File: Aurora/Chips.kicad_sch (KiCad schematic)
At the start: 69 parts, among them J1 UJ20-C-H-C-3-SMT-TR, J2 DM3AT-SF-PEJM5, J3 Conn_Coaxial_Small, SW1 PCM12SMTR, U1 STM32H757BITx, U2 USBLC6-2SC6, U3 TPS2121RUXR, U4 AP63203QWU-7, U5 ICM-45686, U6 ICM-42688-P, U7 BNO085, U8 XBP9X-DMUS-021, U9 MCP23017T-E_SO, Y1 ASEK-32.768KHZ-L-R-T

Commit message: lots of changes; sensors, LEDs, screw terminal blocks
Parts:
- removed J2: DM3AT-SF-PEJM5, DM3AT-SF-PEJM5:HRS_DM3AT-SF-PEJM5, symbol DM3AT-SF-PEJM5:DM3AT-SF-PEJM5
- removed J3: Conn_Coaxial_Small, symbol Connector:Conn_Coaxial_Small
- removed SW1: PCM12SMTR, PCM12SMTR:SW_PCM12SMTR, symbol PCM12SMTR:PCM12SMTR
- removed U9: MCP23017T-E_SO, MCP23017T-E_SO:SOIC127P1030X265-28N, symbol MCP23017T-E_SO:MCP23017T-E_SO
- removed Y1: ASEK-32.768KHZ-L-R-T, ASEK-32.768KHZ-L-R-T:XTAL_ASEK-32.768KHZ-L-R-T, symbol ASEK-32.768KHZ-L-R-T:ASEK-32.768KHZ-L-R-T
- added C22, C23, C24: 4.7uF, Capacitor_SMD:C_1206_3216Metric, symbol Device:C_Small
- added C25, C34, C35, C48: 100nF, Capacitor_SMD:C_1206_3216Metric, symbol Device:C_Small
- added C47: 2.2uF, Capacitor_SMD:C_1206_3216Metric, symbol Device:C_Small
- added C49: 10uF, Capacitor_SMD:C_1206_3216Metric, symbol Device:C_Small
- added C50: 220uF, Capacitor_SMD:C_1206_3216Metric, symbol Device:C_Small
- added D2, D3, D4: LED, LED_SMD:LED_Cree-PLCC4_5x5mm_CW, symbol Device:LED
- added D5: WS2812B-2020, LED_SMD:LED_WS2812B-2020_PLCC4_2.0x2.0mm, symbol LED:WS2812B-2020
- added J16, J3: TSW-104-27-G-D, TSW_104_27_G_D:SAMTEC_TSW-104-27-G-D, symbol TSW-104-27-G-D:TSW-104-27-G-D
- added J6: DM3AT-SF-PEJM5, DM3AT_SF_PEJM5:HRS_DM3AT-SF-PEJM5, symbol DM3AT-SF-PEJM5:DM3AT-SF-PEJM5
- added R13: 82R, Resistor_SMD:R_1206_3216Metric, symbol Device:R_Small
- added R15: 50R, Resistor_SMD:R_1206_3216Metric, symbol Device:R_Small
- added R16: 270R, Resistor_SMD:R_1206_3216Metric, symbol Device:R_Small
- added S1: TL3301NF260QG, TL3301NF260QG:SW_TL3301NF260QG, symbol TL3301NF260QG:TL3301NF260QG
- C1, C10, C11, C12, C13, C14, C15, C16, C17, C18, C19, C2, C20, C21, C26, C27, C28, C29, C3, C30, C31, C32, C33, C36, C37, C38, C39, C4, C40, C43, C44, C45, C46, C5, C6, C7, C8, C9: footprint (none) -> Capacitor_SMD:C_1206_3216Metric
- C41, C42: value 22pF -> 2.2uF; footprint (none) -> Capacitor_SMD:C_1206_3216Metric
- L1: footprint (none) -> Inductor_SMD:L_1206_3216Metric
- R1, R10, R11, R12, R14, R2, R3, R4, R5, R6, R7, R8, R9: footprint (none) -> Resistor_SMD:R_1206_3216Metric
- renumbered Barometer-(U7) to Barometer-(U7)1
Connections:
- net SPI5_MISO is gone; now on net SPI6_MISO: U1.32 (PF8)
- net 3V3: now also U1.154 (VDDLDO), U1.201 (PDR_ON), U1.202 (VDDLDO), U1.91 (VDDLDO), C22.2, C23.2, C24.2, C34.2, C35.2, C48.2, C49.2, C50.2, D5.4 (VDD), J6.4 (VDD), S1.1
- net 7.4V: now also J3.01, R16.1; no longer R4.1, U3.2 (IN2)
- net GND: now also C41.1, U1.20 (VDDSMPS), U1.21 (VFBSMPS), C22.1, C23.1, C24.1, C25.1, C34.1, C35.1, C47.1, C48.1, C49.1, C50.1, D3.1 (K), D5.2 (VSS), J16.08, J6.6 (VSS), J6.P1 (SHIELD), J6.P2 (SHIELD__1), J6.P3 (SHIELD__2), J6.P4 (SHIELD__3), S1.2; no longer C41.2
- net SD_CLK: now also J6.5 (CLK)
- net SD_CMD: now also J6.3 (CMD)
- net SD_DAT0: now also J6.7 (DAT0)
- net SD_DAT1: now also J6.8 (DAT1)
- net SD_DAT2: now also J6.1 (DAT2)
- net SD_DAT3: now also J6.2 (CD/DAT3)
- net USB_VBUS: now also U1.140 (VDD50_USB), C25.2, D2.1 (K); no longer C27.1, J1.A4_B9 (VBUS), J1.A9_B4 (VBUS), U2.5
- net at R14.2: now also S1.3, S1.4
- net at U8.6 (DIO10/PWM0): now also R15.2
- net UART5_RX: now reaches U1.101 (PB12)
- net UART5_TX: now reaches U1.102 (PB13)
- net HDR_GPIO1: now reaches U1.105 (PD8)
- net HDR_GPIO1: now also J3.02
- net HDR_GPIO2: now reaches U1.106 (PD9)
- net HDR_GPIO2: now also J3.03
- net HDR_GPIO3: now reaches U1.107 (PD10)
- net HDR_GPIO3: now also J3.04
- net HDR_GPIO4: now reaches U1.110 (PD11)
- net HDR_GPIO4: now also J3.05
- net HDR_GPIO5: now reaches U1.111 (PD12)
- net HDR_GPIO5: now also J3.06
- net HDR_GPIO6: now reaches U1.112 (PD13)
- net HDR_GPIO6: now also J3.07
- net HDR_GPIO7: now reaches U1.115 (PD14)
- net HDR_GPIO7: now also J3.08
- net HDR_GPIO8: now reaches U1.116 (PD15)
- net HDR_GPIO8: now also J16.01
- net at U1.152 (VCAP): now also C42.2
- net UART8_RX: now reaches U1.197 (PE0)
- net UART8_TX: now reaches U1.198 (PE1)
- net at U1.199 (VCAP): now also C47.2
- net ADC1_SDA: now reaches U1.22 (PF0)
- net ADC1_SDA: now also J16.03
- net ADC1_SCL: now reaches U1.23 (PF1)
- net ADC1_SCL: now also J16.04
- net UART7_RX: now reaches U1.30 (PF6)
- net I2C4_SCL: now reaches U1.70 (PF14)
- net I2C4_SDA: now reaches U1.71 (PF15)
- net at U1.72 (PG0): now also D5.3 (DIN)
- net UART7_TX: now reaches U1.77 (PE8)
- net at U1.89 (VCAP): now also C41.2
- net ADC2_SCL: now reaches U1.93 (PH7)
- net ADC2_SCL: now also J16.06
- net ADC2_SDA: now reaches U1.94 (PH8)
- net ADC2_SDA: now also J16.05
- net MCP_SCL: no longer names the net of U1.192 (PB6)
- net MCP_SDA: no longer names the net of U1.193 (PB7)
- net XIN_32: no longer names the net of U7.27 (XIN32)
- net XIN_32: no longer C41.1
- net XOUT_32: no longer names the net of U7.26 (XOUT32/CLKSEL1)
- net XOUT_32: no longer C42.2
- new net: D4.1 (K), R4.1, U3.2 (IN2)
- new net: D4.2 (A), R16.2
- new net: C27.1, J1.A4_B9 (VBUS), J1.A9_B4 (VBUS), R13.2, U2.5
- new net: D2.2 (A), R13.1
- new net: D3.2 (A), R15.1
- new net 5V: J16.02
- new net PYRO2: J16.07
- no-connect marks 26 -> 28
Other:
- note added: "* NOTE: On the MCU, the XB_TX line RECEIVES data from the XB, while the XB_RX line SENDS data to the XB. Follow the direction the flag points. If the chip is giving you errors, MAKE SURE THE UARTS ARE CORRECT"
- note added: "<- BLUE LED"
- note added: "AMBER LED"
- note added: "Green LED"
- note added: "Header Pins leading to top board"
- note removed: "* NOTE: On the MCU, the XB_TX line RECEIVES data from the XB, while the XB_RX line SENDS data to the XB. Follow the direction the flag points"
- note removed: "--32.768kHz Oscillator-- Oscillator for BNO085 Pin 1 left floating because we are not using it; see datasheet"
- note removed: "16 I/O I2C Expander"
- note removed: "32.768kHz"
- moved on the sheet: U8

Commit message: reorganization
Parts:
- removed J16, J3: TSW-104-27-G-D, TSW_104_27_G_D:SAMTEC_TSW-104-27-G-D, symbol TSW-104-27-G-D:TSW-104-27-G-D
- added J16, J3: PPPC042LFBN-RC, PPPC042LFBN_RC:SULLINS_PPPC042LFBN-RC, symbol PPPC042LFBN-RC:PPPC042LFBN-RC
- added J4, J5: Screw_Terminal_01x08, footprints7:CONN_1715789_PXC, symbol Connector:Screw_Terminal_01x08
- added U9: MCP23017T-E_SO, MCP23017T_E_SO:SOIC127P1030X265-28N, symbol MCP23017T-E_SO:MCP23017T-E_SO
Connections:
- net 5V: now also J3.2, U9.9 (VDD)
- net 7.4V: now also J16.1
- net ADC1_SCL: now also J3.4
- net ADC1_SDA: now also J3.3
- net ADC2_SCL: now also J3.6
- net ADC2_SDA: now also J3.5
- net GND: now also J3.8, U9.10 (VSS)
- net HDR_GPIO1: now also J16.2
- net HDR_GPIO2: now also J16.3
- net HDR_GPIO3: now also J16.4
- net HDR_GPIO4: now also J16.5
- net HDR_GPIO5: now also J16.6
- net HDR_GPIO6: now also J16.7
- net HDR_GPIO7: now also J16.8
- net HDR_GPIO8: now also J3.1
- net PYRO2: now also J3.7
- net EXP_SCL: now reaches U1.192 (PB6)
- net EXP_SCL: now also U9.12 (SCK)
- net EXP_SDA: now reaches U1.193 (PB7)
- net EXP_SDA: now also U9.13 (SDA)
- new net GPIO_A0: J4.8 (Pin_8), U9.21 (GPA0)
- new net GPIO_A1: J4.7 (Pin_7), U9.22 (GPA1)
- new net GPIO_A2: J4.6 (Pin_6), U9.23 (GPA2)
- new net GPIO_A3: J4.5 (Pin_5), U9.24 (GPA3)
- new net GPIO_A4: J4.4 (Pin_4), U9.25 (GPA4)
- new net GPIO_A5: J4.3 (Pin_3), U9.26 (GPA5)
- new net GPIO_A6: J4.2 (Pin_2), U9.27 (GPA6)
- new net GPIO_A7: J4.1 (Pin_1), U9.28 (GPA7)
- new net GPIO_B0: J5.1 (Pin_1), U9.1 (GPB0)
- new net GPIO_B1: J5.2 (Pin_2), U9.2 (GPB1)
- new net GPIO_B2: J5.3 (Pin_3), U9.3 (GPB2)
- new net GPIO_B3: J5.4 (Pin_4), U9.4 (GPB3)
- new net GPIO_B4: J5.5 (Pin_5), U9.5 (GPB4)
- new net GPIO_B5: J5.6 (Pin_6), U9.6 (GPB5)
- new net GPIO_B6: J5.7 (Pin_7), U9.7 (GPB6)
- new net GPIO_B7: J5.8 (Pin_8), U9.8 (GPB7)
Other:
- note added: "16 I/O I2C Expander"
- note added: "Female Header Pins leading to top board"
- note removed: "Header Pins leading to top board"

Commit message: Add files via upload
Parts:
- removed J4, J5: Screw_Terminal_01x08, footprints7:CONN_1715789_PXC, symbol Connector:Screw_Terminal_01x08
- removed U8: XBP9X-DMUS-021, XBP9X-DMUS-021:DIP2200W51P200L3294H279Q20P, symbol XBP9X-DMUS-021:XBP9X-DMUS-021
- added J36: PPPC042LFBN-RC, PPPC042LFBN_RC:SULLINS_PPPC042LFBN-RC, symbol PPPC042LFBN-RC:PPPC042LFBN-RC
- added U13: XBP9X-DMUS-001, XBP9X-DMUS-001:XCVR_XBP9X-DMUS-001, symbol XBP9X-DMUS-001:XBP9X-DMUS-001
- R13: value 82R -> 10k
- R15: value 50R -> 10k
- R16: value 270R -> 10k
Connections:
- net PYRO2 is gone; now on net PYRO2_GPIO: J3.7
- net 3V3: now also U13.2 (VCC)
- net B/R_CLK: now also U13.31 (DIO2/AD2)
- net B/R_MISO: now also U13.17 (DO15/SPI_MISO)
- net B/R_MOSI: now also U13.16 (DO16/SPI_MOSI)
- net GND: now also U13.1 (GND), U13.11 (GND__1), U13.13 (GND__2), U13.22 (GND__3), U13.35 (GND__4), U13.38 (GND__5)
- net HDR_GPIO1: now also U1.130 (PG2), J36.1; no longer J16.2, U1.105 (PD8)
- net HDR_GPIO2: now also U1.131 (PG3), J36.2; no longer J16.3, U1.106 (PD9)
- net HDR_GPIO3: now also U1.134 (PG4), J36.3; no longer J16.4, U1.107 (PD10)
- net HDR_GPIO4: now also U1.135 (PG5), J36.4; no longer J16.5, U1.110 (PD11)
- net HDR_GPIO5: now also U1.136 (PG6), J36.5; no longer J16.6, U1.111 (PD12)
- net XBP_ATTN: now also U13.36 (RF_PAD)
- net XBP_CS: now also U13.30 (DIO3/AD3)
- net XB_RX: now also U13.4 (DIO14/DIN/~{CONFIG})
- net XB_TX: now also U13.3 (DIO13/DOUT)
- net at R15.2: now also U13.7 (DIO10/RSSI/PWM0)
- net SPKG: now reaches U1.137 (PG7)
- net SPKG: now also J36.6
- net SLN_1: now reaches U1.138 (PG8)
- net SLN_1: now also J36.7
- net MISC_GPIO1: now reaches U1.146 (PA8)
- net MISC_GPIO2: now reaches U1.147 (PA9)
- net MISC_GPIO3: now reaches U1.148 (PA10)
- net MISC_GPIO4: now reaches U1.149 (PA11)
- net PYRO1_GPIO: now reaches U1.176 (PD6)
- net PYRO1_GPIO: now also J3.1
- net PYRO2_GPIO: now reaches U1.177 (PD7)
- net SLN_2: now reaches U1.180 (PG9)
- net SLN_2: now also J36.8
- net HDR_GPIO6 renamed SERVO6
- net HDR_GPIO7 renamed SERVO7
- net HDR_GPIO8: no longer names the net of U1.116 (PD15)
- net HDR_GPIO8: no longer J3.1
- new net SERVO1: J16.2, U1.105 (PD8)
- new net SERVO2: J16.3, U1.106 (PD9)
- new net SERVO3: J16.4, U1.107 (PD10)
- new net SERVO4: J16.5, U1.110 (PD11)
- new net SERVO5: J16.6, U1.111 (PD12)
- no-connect marks 28 -> 21
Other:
- note added: "Header pins"
- moved on the sheet: C48, C49, C50, D3, J16, J3, R15

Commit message: Boot0 and NRST pins
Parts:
- added R21: 10kR, Resistor_SMD:R_1206_3216Metric, symbol Device:R_Small
- added S2: TL3301NF260QG, TL3301NF260QG:SW_TL3301NF260QG, symbol TL3301NF260QG:TL3301NF260QG
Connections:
- net 3V3: now also R21.2
- net GND: now also R14.2, S2.2; no longer S1.2
- net at U1.194 (BOOT0): now also S1.3, S1.4; no longer R14.1
- net at U1.37 (NRST): now also S2.3, S2.4
- new net: R21.1, S2.1
- new net: R14.1, S1.2
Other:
- moved on the sheet: R14, S1

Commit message: All CS pins include 10k pullups on SPI buses
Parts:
- added R22, R23, R24: 10kR, Resistor_SMD:R_1206_3216Metric, symbol Device:R_Small
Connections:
- net 3V3: now also R22.1, R23.1, R24.1
- net BMP_CS: now also R23.2
- net STM_CSN: now also R22.2
- net XBP_CS: now also R24.2

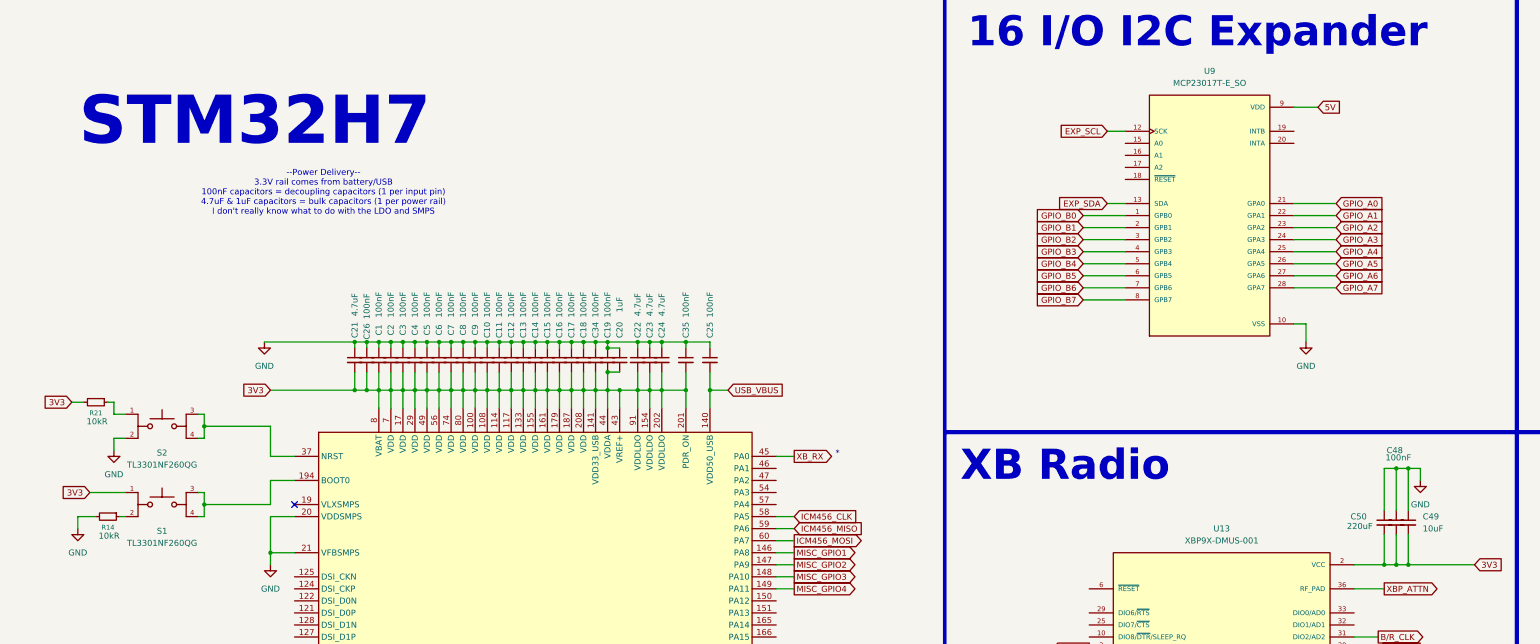
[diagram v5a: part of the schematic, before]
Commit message: some changes to the reset and boot pins, wip
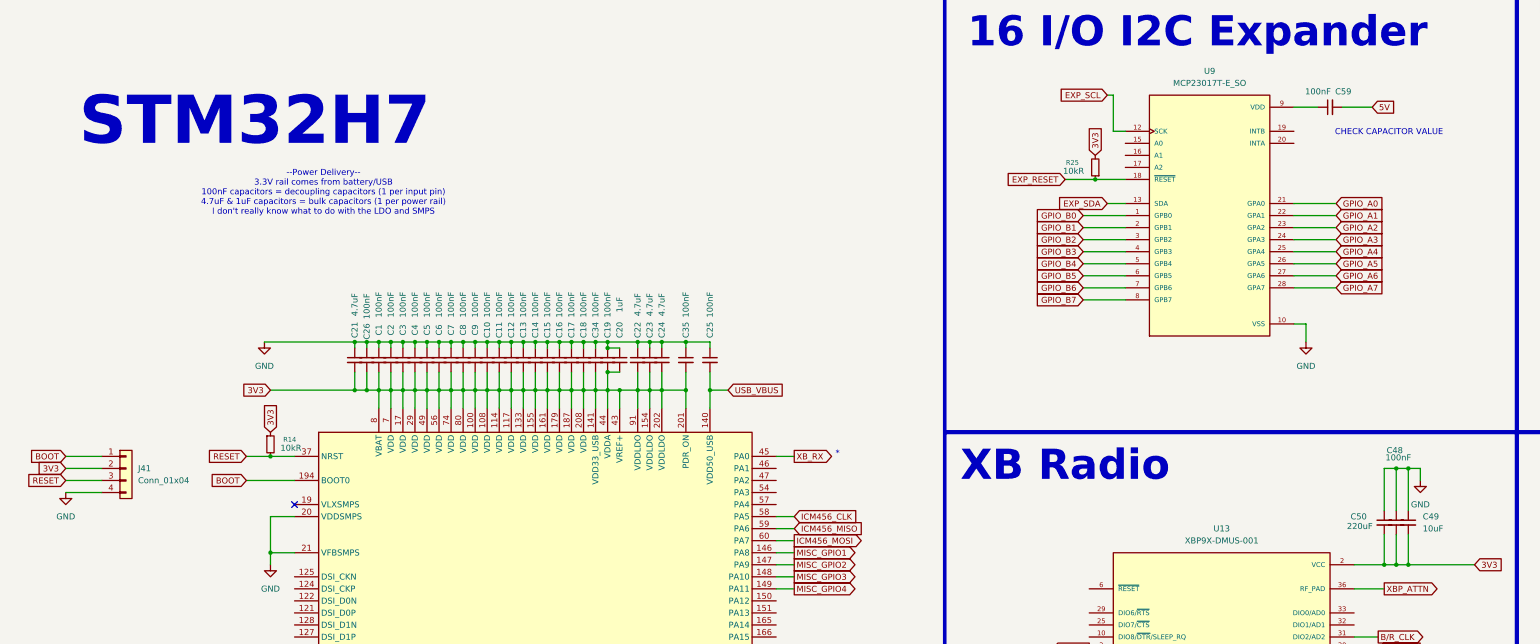
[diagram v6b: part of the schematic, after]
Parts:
- removed R21: 10kR, Resistor_SMD:R_1206_3216Metric, symbol Device:R_Small
- removed S1, S2: TL3301NF260QG, TL3301NF260QG:SW_TL3301NF260QG, symbol TL3301NF260QG:TL3301NF260QG
- added C59: 100nF, Capacitor_SMD:C_1206_3216Metric, symbol Device:C_Small
- added J41: Conn_01x04, Connector_JST:JST_PH_S4B-PH-SM4-TB_1x04-1MP_P2.00mm_Horizontal, symbol Connector_Generic:Conn_01x04
- added R25: 10kR, Resistor_SMD:R_1206_3216Metric, symbol Device:R_Small
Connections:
- net 3V3: now also R14.1, J41.2 (Pin_2), R25.2
- net 5V: now also C59.2; no longer U9.9 (VDD)
- net GND: now also J41.4 (Pin_4); no longer R14.2
- net BOOT: now reaches U1.194 (BOOT0)
- net BOOT: now also J41.1 (Pin_1)
- net RESET: now reaches U1.37 (NRST)
- net RESET: now also R14.2, J41.3 (Pin_3)
- net EXP_RESET: now reaches U9.18 (~{RESET})
- net EXP_RESET: now also R25.1
- new net: C59.1, U9.9 (VDD)
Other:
- note added: "CHECK CAPACITOR VALUE"
